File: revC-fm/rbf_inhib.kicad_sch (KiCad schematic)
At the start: 12 parts, among them Q2 MMDT5551-7-F, Q21 MMDT3946, Q22 BSZ180P03NS3GATMA1, Q23 BSZ180P03NS3GATMA1

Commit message: almost done!!!!!
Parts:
- Q22, Q23: value BSZ180P03NS3GATMA1 -> BSZ180
- R88: value 100k -> 220k
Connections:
- net IN_HI renamed IN
- net IN_LO renamed OUT
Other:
- note added: "Push-Pull Gate Driver"
- note added: "RBF Inhibit"
- note added: "RBF Logic Inversion"
- moved on the sheet: C36, Q21A, Q21B, Q23, Q2A, R141, R251, R54, R57, R88

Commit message: updated fab files
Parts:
- C36: Manufacturer (none) -> TDK; Mfr. Part No (none) -> CGA2B3X7R1H104K050BE
- Q2: Manufacturer (none) -> Diodes Incorporated; Mfr. Part No (none) -> MMDT5551-7-F
- Q21: Manufacturer (none) -> Diodes Incorporated
- Q22, Q23: Manufacturer (none) -> Infineon
- R110: renamed from R251; value 1Meg -> 10Meg; Manufacturer (none) -> Stackpole Electronics; Mfr. Part No (none) -> RMCF0402FT10M0
- R141, R87: Manufacturer (none) -> Panasonic; Mfr. Part No (none) -> ERJ-2GEJ102X
- R54: Manufacturer (none) -> Stackpole Electronics; Mfr. Part No (none) -> RMCF0603ZT0R00
- R57: Manufacturer (none) -> Stackpole Electronics; Mfr. Part No (none) -> RMCF0402FT1M00
- R88: Manufacturer (none) -> Stackpole Electronics; Mfr. Part No (none) -> RMCF0402FT220K
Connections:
- net at Q2.2 (B1), Q2.2 (B1), R110.2: now also Q2.6 (C1)
- no-connect marks 1 -> 0
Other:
- moved on the sheet: Q2A, R110

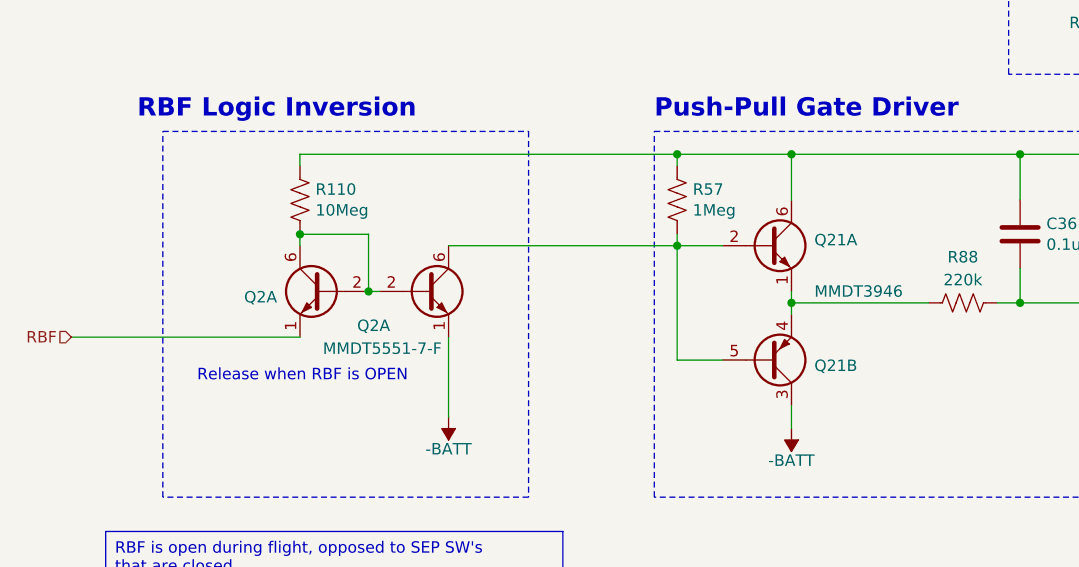
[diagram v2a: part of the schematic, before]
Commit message: updated per review, improved docs
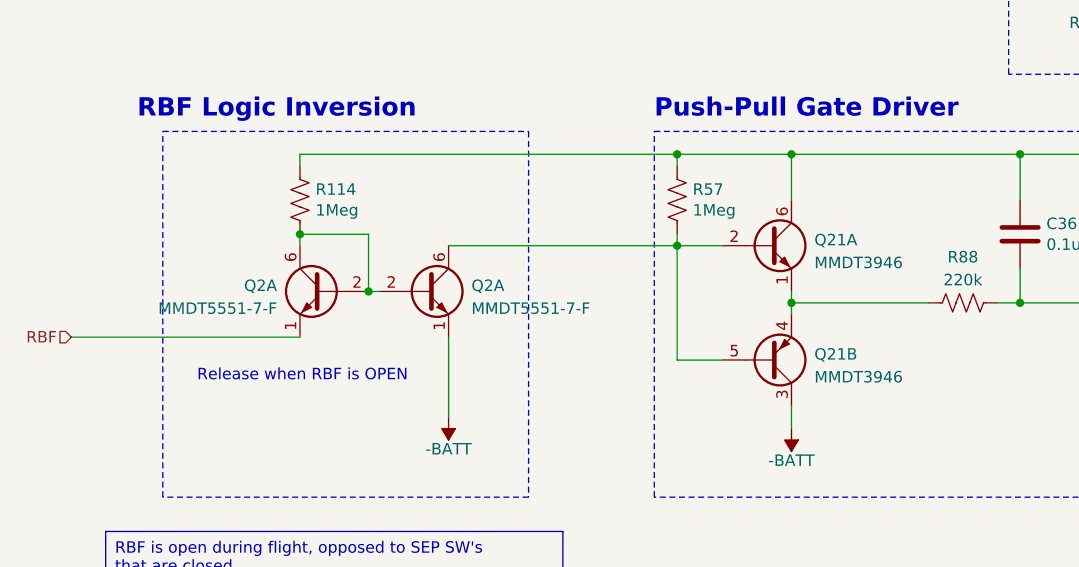
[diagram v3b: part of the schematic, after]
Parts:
- R114: renamed from R110; value 10Meg -> 1Meg; Mfr. Part No RMCF0402FT10M0 -> RMCF0402FT1M00
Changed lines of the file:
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@@
+    (stroke (width 0) (type default))
+  )
+  (wire (pts (xy 48.26 73.66) (xy 157.48 73.66))
     (stroke (width 0) (type default))
   )
@@
   )
   (wire (pts (xy 88.9 110.49) (xy 114.3 110.49))
-    (stroke (width 0) (type default))
-  )
-  (wire (pts (xy 48.26 73.66) (xy 157.48 73.66))
     (stroke (width 0) (type default))
   )
@@
   (symbol (lib_id "Transistor_BJT:MMDT5551") (at 74.93 115.57 0) (mirror y) (unit 1)
     (in_bom yes) (on_board yes) (dnp no) (fields_autoplaced)
-    (property "Reference" "Q2" (at 69.85 116.205 0)
-      (effects (font (size 1.27 1.27)) (justify left))
-    )
-    (property "Value" "MMDT5551-7-F" (at 71.12 109.22 0)
-      (effects (font (size 1.27 1.27)) (justify left) hide)
+    (property "Reference" "Q2" (at 69.85 114.935 0)
+      (effects (font (size 1.27 1.27)) (justify left))
+    )
+    (property "Value" "MMDT5551-7-F" (at 69.85 117.475 0)
+      (effects (font (size 1.27 1.27)) (justify left))
     )
     (property "Footprint" "Package_TO_SOT_SMD:SOT-363_SC-70-6" (at 69.85 113.03 0)
@@
     )
     (property "Manufacturer" "Diodes Incorporated" (at 74.93 115.57 0)
+      (effects (font (size 1.27 1.27)) hide)
+    )
+    (property "Description" "TRANS 2NPN 160V 0.2A SOT363" (at 74.93 115.57 0)
       (effects (font (size 1.27 1.27)) hide)
     )
@@
       (effects (font (size 1.27 1.27)) hide)
     )
+    (property "Description" "RES 220K OHM 1% 1/16W 0402" (at 146.05 116.84 0)
+      (effects (font (size 1.27 1.27)) hide)
+    )
     (pin "1")
     (pin "2")
@@
         )
         (path "/d1441985-7b63-4bf8-a06d-c70da2e3b78b/00000000-0000-0000-0000-00005cec5dde/88093887-0c33-45d6-99b0-9b95992083af"
-          (reference "R112") (unit 1)
+          (reference "R116") (unit 1)
         )
       )
@@
       (effects (font (size 1.27 1.27)) hide)
     )
+    (property "Description" "RES 0 OHM JUMPER 1/10W 0603" (at 187.96 86.36 0)
+      (effects (font (size 1.27 1.27)) hide)
+    )
     (pin "1")
     (pin "2")
@@
         )
         (path "/d1441985-7b63-4bf8-a06d-c70da2e3b78b/00000000-0000-0000-0000-00005cec5dde/88093887-0c33-45d6-99b0-9b95992083af"
-          (reference "R109") (unit 1)
+          (reference "R113") (unit 1)
         )
       )
@@
       (effects (font (size 1.27 1.27)) hide)
     )
+    (property "Description" "MOSFET P-CH 30V 9A/39.6A TSDSON" (at 163.83 73.66 0)
+      (effects (font (size 1.27 1.27)) hide)
+    )
     (pin "1")
     (pin "4")
@@
   )
   (symbol (lib_id "Transistor_BJT:MMDT5551") (at 86.36 115.57 0) (unit 1)
-    (in_bom yes) (on_board yes) (dnp no)
-    (property "Reference" "Q2" (at 78.74 119.38 0)
-      (effects (font (size 1.27 1.27)) (justify left))
-    )
-    (property "Value" "MMDT5551-7-F" (at 74.93 121.92 0)
+    (in_bom yes) (on_board yes) (dnp no) (fields_autoplaced)
+    (property "Reference" "Q2" (at 91.44 114.935 0)
+      (effects (font (size 1.27 1.27)) (justify left))
+    )
+    (property "Value" "MMDT5551-7-F" (at 91.44 117.475 0)
       (effects (font (size 1.27 1.27)) (justify left))
     )
@@
     )
     (property "Manufacturer" "Diodes Incorporated" (at 86.36 115.57 0)
+      (effects (font (size 1.27 1.27)) hide)
+    )
+    (property "Description" "TRANS 2NPN 160V 0.2A SOT363" (at 86.36 115.57 0)
       (effects (font (size 1.27 1.27)) hide)
     )
@@
   )
   (symbol (lib_id "Transistor_BJT:MMDT3946") (at 124.46 123.19 0) (mirror x) (unit 2)
-    (in_bom yes) (on_board yes) (dnp no)
-    (property "Reference" "Q21" (at 129.54 123.825 0)
-      (effects (font (size 1.27 1.27)) (justify left))
-    )
-    (property "Value" "MMDT3946" (at 129.54 121.285 0)
-      (effects (font (size 1.27 1.27)) (justify left) hide)
+    (in_bom yes) (on_board yes) (dnp no) (fields_autoplaced)
+    (property "Reference" "Q21" (at 129.54 122.555 0)
+      (effects (font (size 1.27 1.27)) (justify left))
+    )
+    (property "Value" "MMDT3946" (at 129.54 125.095 0)
+      (effects (font (size 1.27 1.27)) (justify left))
     )
     (property "Footprint" "Package_TO_SOT_SMD:SOT-363_SC-70-6" (at 129.54 125.73 0)
@@
     )
     (property "Manufacturer" "Diodes Incorporated" (at 124.46 123.19 0)
+      (effects (font (size 1.27 1.27)) hide)
+    )
+    (property "Description" "TRANS NPN/PNP 40V 0.2A SOT363" (at 124.46 123.19 0)
       (effects (font (size 1.27 1.27)) hide)
     )
@@
   )
   (symbol (lib_id "Transistor_BJT:MMDT3946") (at 124.46 110.49 0) (unit 1)
-    (in_bom yes) (on_board yes) (dnp no)
+    (in_bom yes) (on_board yes) (dnp no) (fields_autoplaced)
     (property "Reference" "Q21" (at 129.54 109.855 0)
       (effects (font (size 1.27 1.27)) (justify left))
     )
-    (property "Value" "MMDT3946" (at 129.54 115.57 0)
+    (property "Value" "MMDT3946" (at 129.54 112.395 0)
       (effects (font (size 1.27 1.27)) (justify left))
     )
@@
     )
     (property "Manufacturer" "Diodes Incorporated" (at 124.46 110.49 0)
+      (effects (font (size 1.27 1.27)) hide)
+    )
+    (property "Description" "TRANS NPN/PNP 40V 0.2A SOT363" (at 124.46 110.49 0)
       (effects (font (size 1.27 1.27)) hide)
     )
@@
       (effects (font (size 1.27 1.27)) hide)
     )
+    (property "Description" "RES 1M OHM 1% 1/16W 0402" (at 114.3 105.41 0)
+      (effects (font (size 1.27 1.27)) hide)
+    )
     (pin "1")
     (pin "2")
@@
         )
         (path "/d1441985-7b63-4bf8-a06d-c70da2e3b78b/00000000-0000-0000-0000-00005cec5dde/88093887-0c33-45d6-99b0-9b95992083af"
-          (reference "R111") (unit 1)
+          (reference "R115") (unit 1)
         )
       )
@@
       (effects (font (size 1.27 1.27)) hide)
     )
+    (property "Description" "RES SMD 1K OHM 5% 1/10W 0402" (at 170.18 86.36 0)
+      (effects (font (size 1.27 1.27)) hide)
+    )
     (pin "1")
     (pin "2")
@@
         )
         (path "/d1441985-7b63-4bf8-a06d-c70da2e3b78b/00000000-0000-0000-0000-00005cec5dde/88093887-0c33-45d6-99b0-9b95992083af"
-          (reference "R108") (unit 1)
+          (reference "R112") (unit 1)
         )
       )
@@
       (effects (font (size 1.27 1.27)) hide)
     )
+    (property "Description" "MOSFET P-CH 30V 9A/39.6A TSDSON" (at 170.18 64.77 0)
+      (effects (font (size 1.27 1.27)) hide)
+    )
     (pin "1")
     (pin "4")
@@
         )
         (path "/d1441985-7b63-4bf8-a06d-c70da2e3b78b/00000000-0000-0000-0000-00005cec5dde/88093887-0c33-45d6-99b0-9b95992083af"
-          (reference "#PWR0106") (unit 1)
+          (reference "#PWR0111") (unit 1)
         )
       )
@@
         )
         (path "/d1441985-7b63-4bf8-a06d-c70da2e3b78b/00000000-0000-0000-0000-00005cec5dde/88093887-0c33-45d6-99b0-9b95992083af"
-          (reference "#PWR0105") (unit 1)
+          (reference "#PWR0110") (unit 1)
         )
       )
@@
       (effects (font (size 1.27 1.27)) hide)
     )
+    (property "Description" "RES SMD 1K OHM 5% 1/10W 0402" (at 163.83 86.36 0)
+      (effects (font (size 1.27 1.27)) hide)
+    )
     (pin "1")
     (pin "2")
@@
         )
         (path "/d1441985-7b63-4bf8-a06d-c70da2e3b78b/00000000-0000-0000-0000-00005cec5dde/88093887-0c33-45d6-99b0-9b95992083af"
-          (reference "R107") (unit 1)
+          (reference "R111") (unit 1)
         )
       )
@@
   (symbol (lib_id "Device:R_US") (at 72.39 105.41 0) (unit 1)
     (in_bom yes) (on_board yes) (dnp no)
-    (property "Reference" "R110" (at 74.1172 104.2416 0)
-      (effects (font (size 1.27 1.27)) (justify left))
-    )
-    (property "Value" "10Meg" (at 74.1172 106.553 0)
+    (property "Reference" "R114" (at 74.1172 104.2416 0)
+      (effects (font (size 1.27 1.27)) (justify left))
+    )
+    (property "Value" "1Meg" (at 74.1172 106.553 0)
       (effects (font (size 1.27 1.27)) (justify left))
     )
@@
       (effects (font (size 1.27 1.27)) hide)
     )
-    (property "Mfr. Part No" "RMCF0402FT10M0" (at 72.39 105.41 0)
+    (property "Mfr. Part No" "RMCF0402FT1M00" (at 72.39 105.41 0)
       (effects (font (size 1.27 1.27)) hide)
     )
@@
       (effects (font (size 1.27 1.27)) hide)
     )
-    (pin "1")
-    (pin "2")
-    (instances
-      (project "mainboard"
-        (path "/d1441985-7b63-4bf8-a06d-c70da2e3b78b/00000000-0000-0000-0000-00005cec5dde/88093887-0c33-45d6-99b0-9b95992083af"
-          (reference "R110") (unit 1)
+    (property "Description" "RES 1M OHM 1% 1/16W 0402" (at 72.39 105.41 0)
+      (effects (font (size 1.27 1.27)) hide)
+    )
+    (pin "1")
+    (pin "2")
+    (instances
+      (project "mainboard"
+        (path "/d1441985-7b63-4bf8-a06d-c70da2e3b78b/00000000-0000-0000-0000-00005cec5dde/88093887-0c33-45d6-99b0-9b95992083af"
+          (reference "R114") (unit 1)
         )
       )
@@
     )
     (property "Manufacturer" "TDK" (at 152.4 109.22 0)
+      (effects (font (size 1.27 1.27)) hide)
+    )
+    (property "Description" "CAP CER 0.1UF 50V X7R 0402" (at 152.4 109.22 0)
       (effects (font (size 1.27 1.27)) hide)
     )
@@
         )
         (path "/d1441985-7b63-4bf8-a06d-c70da2e3b78b/00000000-0000-0000-0000-00005cec5dde/88093887-0c33-45d6-99b0-9b95992083af"
-          (reference "C59") (unit 1)
-        )
-      )
+          (reference "C60") (unit 1)
+        )
+      )
